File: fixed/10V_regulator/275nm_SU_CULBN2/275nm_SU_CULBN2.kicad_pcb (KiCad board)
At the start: 2 copper layers, 25.4 x 20 mm, 18 parts, among them J1 Conn_01x04, J2 Conn_01x04, M1 MountingHole_2.5mm_Pad, M2 MountingHole_2.5mm_Pad, M3 MountingHole_2.5mm_Pad, M4 MountingHole_2.5mm_Pad, Q1 MMBT5551L, U1 TPS61222DCK, U2 LMV321

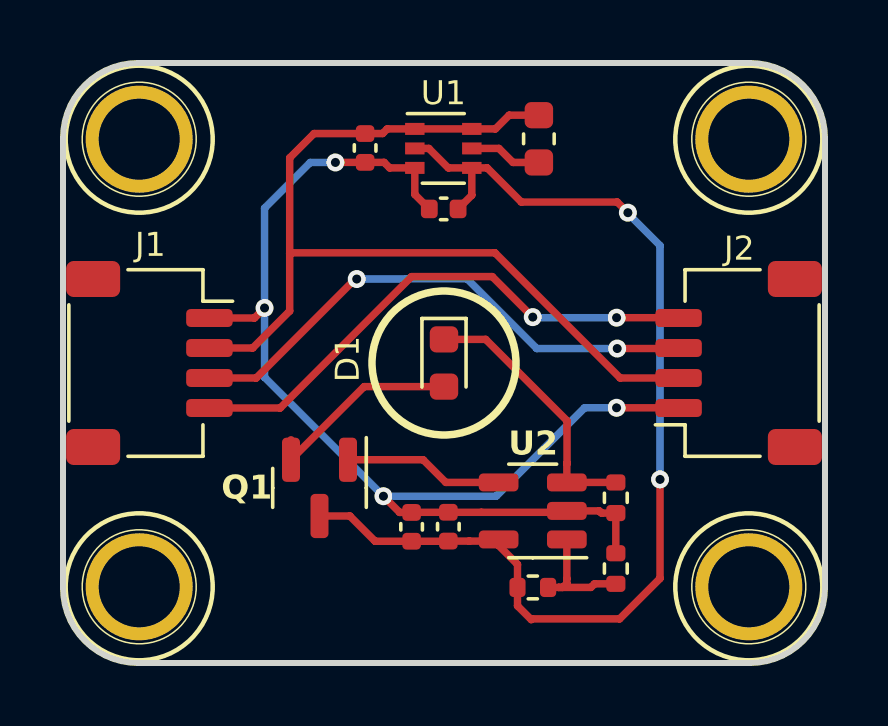
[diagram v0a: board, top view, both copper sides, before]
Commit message: Working on 10V, fixed, 275nm LED layout.
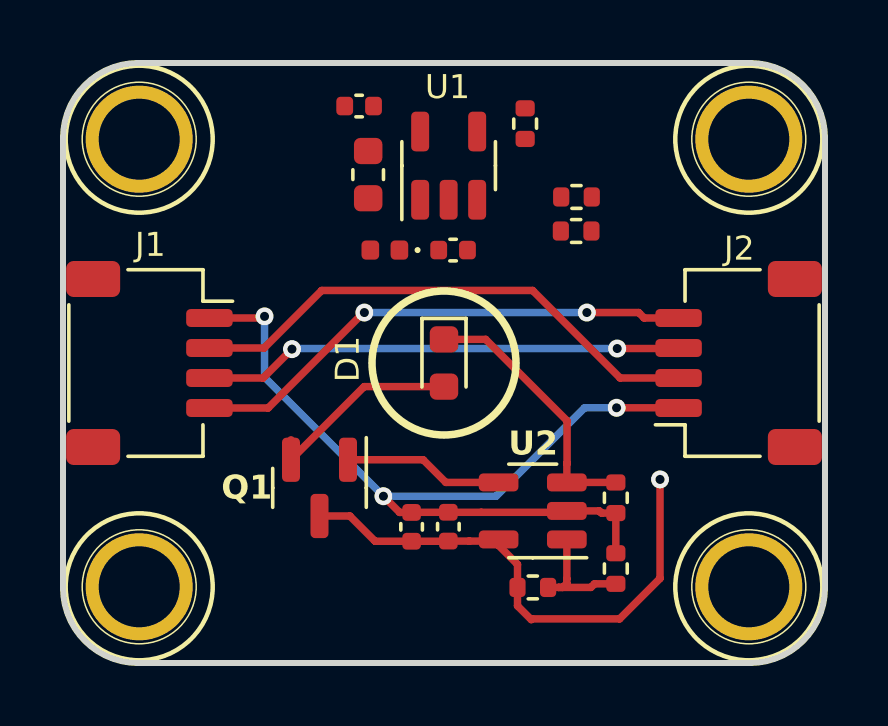
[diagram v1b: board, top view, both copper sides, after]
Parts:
- added D2: D_Schottky, Diode_SMD:D_0402_1005Metric, F.Cu at (60.7, 56.2)
- added R4: 14k, Resistor_SMD:R_0402_1005Metric, F.Cu at (65.4, 52.0)
- added R5: 14k, Resistor_SMD:R_0402_1005Metric, F.Cu at (67.1, 55.6)
- added R6: 2k, Resistor_SMD:R_0402_1005Metric, F.Cu at (67.1, 54.5)
- C1, C2, C4: value 10uF -> 1uF
- L1: value 4.7uF -> 22uF
- R2: value 20k -> 24k
- R3: value 1k -> 590
- U1: value TPS61222DCK -> AP3012; footprint Package_TO_SOT_SMD:SOT-363_SC-70-6 -> Package_TO_SOT_SMD:SOT-23-5
- moved L1 5.81 mm to (60.2, 53.7)
- moved C1 1.41 mm to (59.9, 51.4), turned to 180 degrees
- moved C2 1.41 mm to (63.0, 56.2), turned to 180 degrees
- moved U1 0.60 mm to (62.9, 53.4), turned to 90 degrees
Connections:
- C2 pad 2: /5V -> /10V
- C3 pad 1: /5V -> /10V
- C4 pad 1: /5V -> /10V
- L1 pad 2: /VL -> Net-(D2-A)
- Q1 pad 3: /5V -> /10V
- R2 pad 1: /5V -> /10V
- U1 pad 1: /VIN -> Net-(D2-A)
- U1 pad 2: /5V -> GND
- U1 pad 3: GND -> Net-(U1-FB)
- U1 pad 4: /5V -> Net-(U1-~{SHDN})
- U1 pad 5: /VL -> /VIN
- U2 pad 5: /5V -> /10V
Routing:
- net /5V: track 37.0 -> 0.00 mm, vias 2 -> 0
- net /10V: track 0.00 -> 18.1 mm, vias 0 -> 1
- net /VIN: track 31.7 -> 17.4 mm
- net GND: track 40.8 -> 29.7 mm, vias 4 -> 3
- net /VL: track 2.43 -> 0.00 mm
- net /SDA: track 17.9 -> 15.9 mm
- net /SCL: track 17.9 -> 16.9 mm

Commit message: Worked on 10V fixed 257nm LED board.
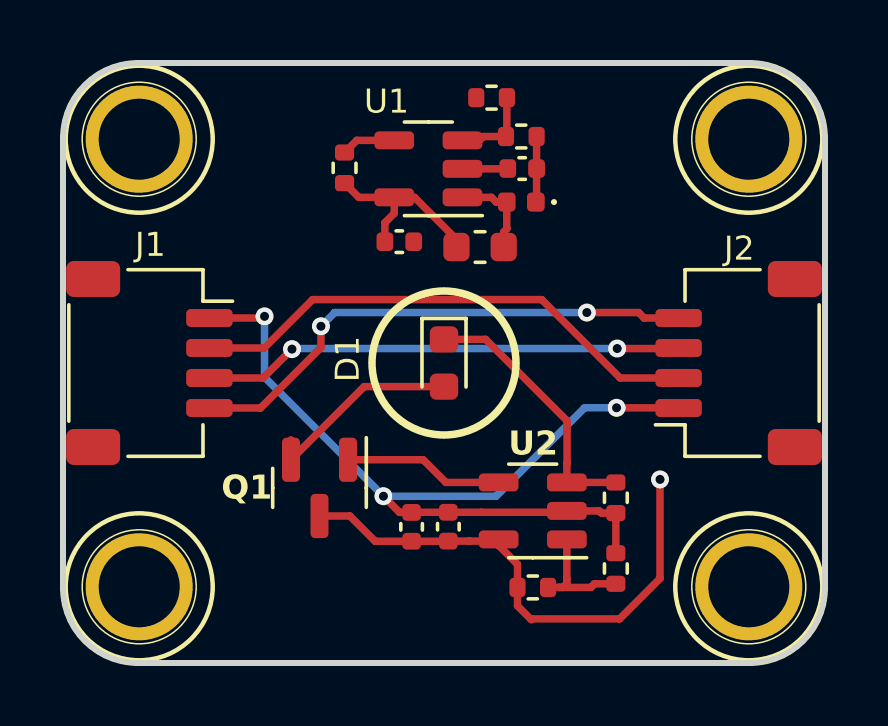
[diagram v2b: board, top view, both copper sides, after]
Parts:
- moved R4 6.20 mm to (59.4, 53.5), turned to 90 degrees
- moved D2 4.82 mm to (65.3, 54.6)
- moved C1 4.72 mm to (61.2, 56.0)
- moved L1 4.44 mm to (63.9, 56.1), turned to 0 degrees
- moved R6 4.36 mm to (64.3, 51.2), turned to 180 degrees
- moved R5 3.64 mm to (65.3, 52.5)
- moved C2 3.56 mm to (65.3, 53.5), turned to 0 degrees
- moved U1 0.68 mm to (62.2, 53.5), turned to 180 degrees
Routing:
- net /VIN: track 17.4 -> 23.6 mm
- net Net-(D2-A): track 0.00 -> 3.08 mm
- net Net-(U1-FB): track 0.00 -> 2.81 mm
- net /10V: track 18.1 -> 20.3 mm
- net Net-(U1-~{SHDN}): track 0.00 -> 1.82 mm
- net GND: track 29.7 -> 31.3 mm

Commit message: Worked on 275nm LED board.
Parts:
- D1: value LED -> LED_Pad; footprint LED_SMD:LED_0603_1608Metric -> LED_1414:LED_1414
- moved Q1 1.72 mm to (58.2, 65.8)
- moved R6 1.47 mm to (62.8, 50.9)
- moved L1 0.46 mm to (64.2, 55.8)
- moved C1 0.46 mm to (61.2, 55.5)
- moved C2 0.38 mm to (65.5, 53.2)
- moved D2 0.38 mm to (65.5, 54.3)
- moved R4 0.38 mm to (59.6, 53.2)
- moved R5 0.38 mm to (65.5, 52.1)
- moved U1 0.38 mm to (62.4, 53.2)
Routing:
- net GND: track 31.3 -> 49.7 mm, vias 3 -> 4
- net /10V: track 20.3 -> 32.3 mm, vias 1 -> 2
- net Net-(D1-K): track 8.92 -> 13.8 mm
- net /VIN: track 23.6 -> 25.9 mm, vias 0 -> 2
- net Net-(D1-A): track 6.77 -> 8.23 mm
- net Net-(Q1-B): track 5.40 -> 6.15 mm
- added copper zone on F.Cu, net Net-(D1-A)
- added copper zone on F.Cu, net Net-(D1-K)
- added copper zone on F.Cu, net unconnected-(D1-PAD-Pad3)
